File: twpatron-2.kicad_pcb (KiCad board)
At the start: 4 copper layers, 38.1 x 21 mm, 12 parts, among them J1 Conn_01x04, J3 SMP-straight-19S141-40ML5, J6 Conn_01x04, U1 MM5800, U2 MM5800, U3 MM5800, U4 MM5800

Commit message: a full draft of pcb is essentially done now
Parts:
- added ?: , , F.Cu at (149.4, 74.3)
- J3: footprint rosenberger-smp:rosenberger-19S141-40ML5 -> molex-smp:MOLEX_85305-0232

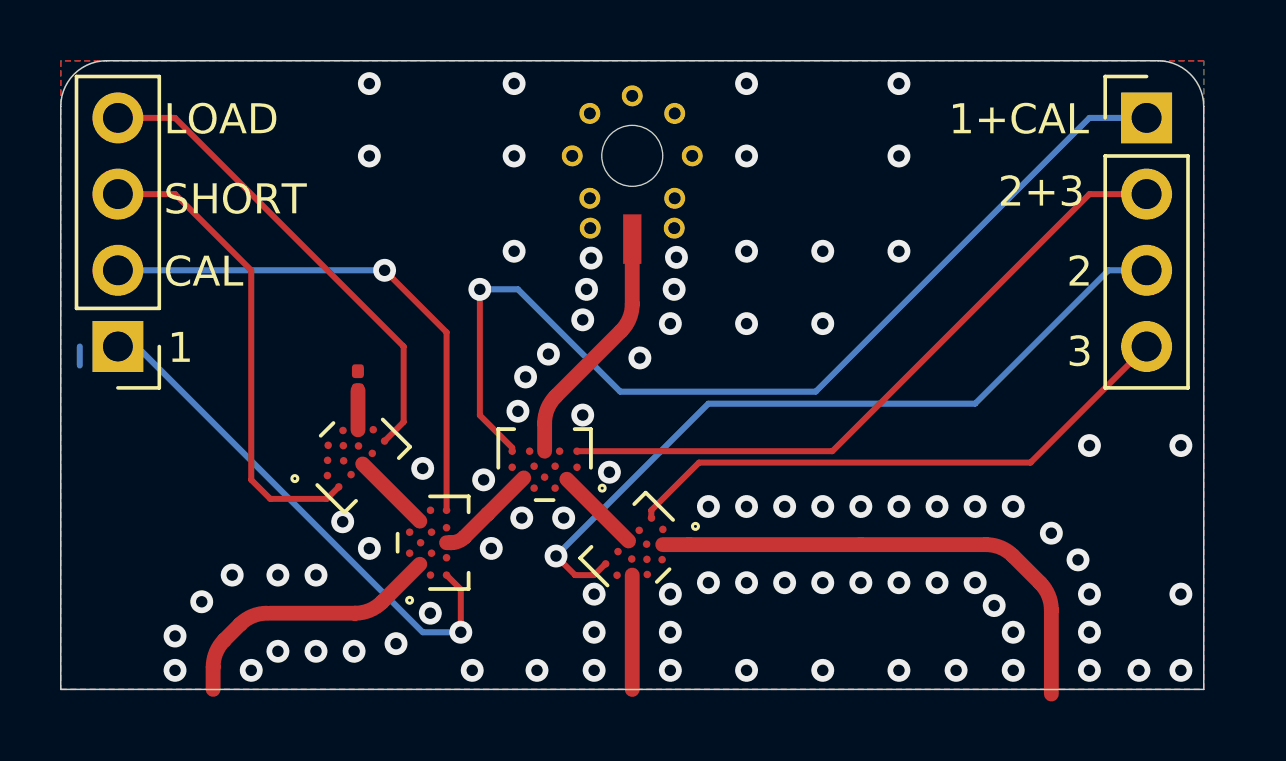
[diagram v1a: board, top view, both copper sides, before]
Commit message: added jaws design, tweaked mechanical for M2.5 screws
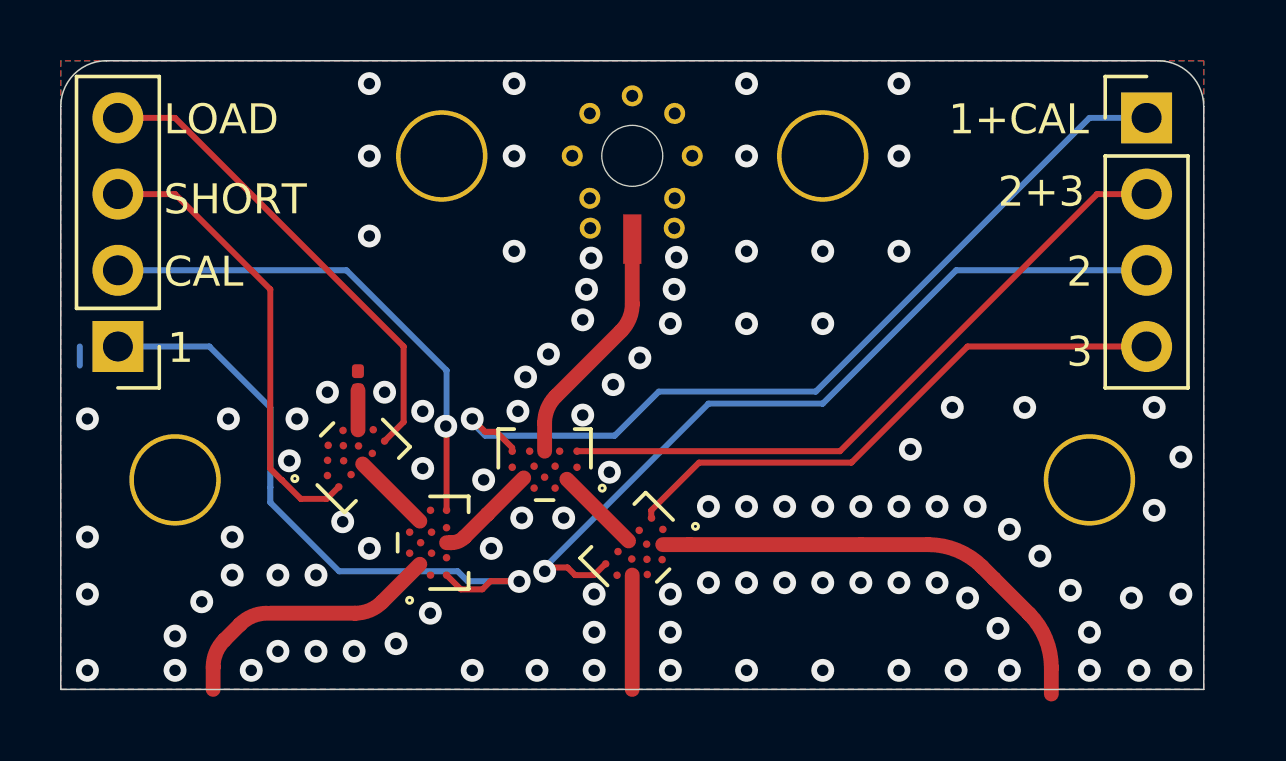
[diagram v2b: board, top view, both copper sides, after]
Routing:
- net Net-(J1-Pin_1): track 33.3 -> 29.0 mm
- net Net-(J6-Pin_1): track 18.1 -> 21.8 mm
- net unconnected-(U2-RF1-PadC3): track 16.9 -> 15.9 mm
- net Net-(J1-Pin_3): track 25.7 -> 26.6 mm
- net Net-(J6-Pin_2): track 17.7 -> 17.0 mm
- net Net-(J6-Pin_3): track 15.8 -> 15.2 mm
- net GND: vias 87 -> 103

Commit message: changed to stackup like JAWS
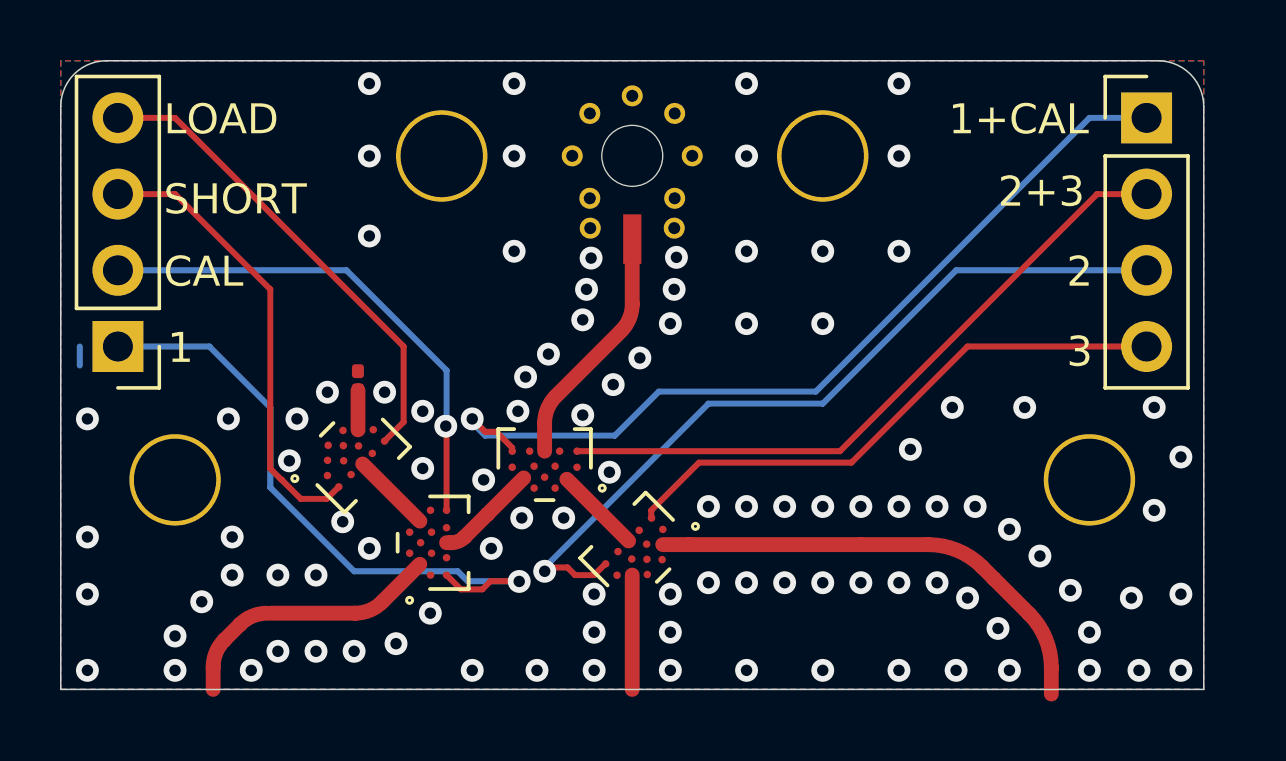
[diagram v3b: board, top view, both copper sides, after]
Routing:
- removed copper zone on In1.Cu, net GND
- removed copper zone on In2.Cu, net GND
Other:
- copper layers 4 -> 2
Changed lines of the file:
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@@
 	(generator_version "9.0")
 	(general
-		(thickness 1.125199)
+		(thickness 0.598)
 		(legacy_teardrops no)
 	)
@@
 	(layers
 		(0 "F.Cu" signal "Top Layer")
-		(4 "In1.Cu" signal "Mid-Layer 1")
-		(6 "In2.Cu" signal "Mid-Layer 2")
 		(2 "B.Cu" signal "Bottom Layer")
 		(9 "F.Adhes" user "F.Adhesive")
@@
 			(layer "F.Mask"
 				(type "Top Solder Mask")
+				(color "Green")
 				(thickness 0.01)
 			)
@@
 			(layer "dielectric 1"
 				(type "core")
-				(thickness 0.321733)
-				(material "FR4")
-				(epsilon_r 4.5)
-				(loss_tangent 0.02)
-			)
-			(layer "In1.Cu"
-				(type "copper")
-				(thickness 0.035)
-			)
-			(layer "dielectric 2"
-				(type "prepreg")
-				(thickness 0.321733)
-				(material "FR4")
-				(epsilon_r 4.5)
-				(loss_tangent 0.02)
-			)
-			(layer "In2.Cu"
-				(type "copper")
-				(thickness 0.035)
-			)
-			(layer "dielectric 3"
-				(type "core")
-				(thickness 0.321733)
-				(material "FR4")
-				(epsilon_r 4.5)
-				(loss_tangent 0.02)
+				(color "FR4 natural")
+				(thickness 0.508)
+				(material "RO4350B")
+				(epsilon_r 3.48)
+				(loss_tangent 0)
 			)
 			(layer "B.Cu"
@@
 			(layer "B.Mask"
 				(type "Bottom Solder Mask")
+				(color "Green")
 				(thickness 0.01)
 			)
@@
 	)
 	(segment
-		(start 137.3111 85.3176)
-		(end 137.3117 85.317)
-		(width 0.2)
-		(layer "B.Cu")
-		(net 7)
-	)
-	(segment
-		(start 145.608069 88.450092)
-		(end 145.599777 88.4418)
+		(start 140.1051 88.1116)
+		(end 137.3111 85.3176)
 		(width 0.2)
 		(layer "B.Cu")
@@
 	)
 	(segment
-		(start 137.3111 85.817422)
-		(end 137.3111 85.3176)
+		(start 143.8897 88.4418)
+		(end 143.5595 88.1116)
 		(width 0.2)
 		(layer "B.Cu")
@@
 	)
 	(segment
-		(start 139.605278 88.1116)
-		(end 137.3111 85.817422)
+		(start 145.608069 88.450092)
+		(end 145.599777 88.4418)
 		(width 0.2)
 		(layer "B.Cu")
@@
 	)
 	(segment
-		(start 143.5595 88.1116)
-		(end 139.605278 88.1116)
+		(start 137.3111 85.3176)
+		(end 137.3117 85.317)
 		(width 0.2)
 		(layer "B.Cu")
@@
 	)
 	(segment
-		(start 135.2791 80.6186)
-		(end 132.2311 80.6186)
+		(start 130.9611 81.2536)
+		(end 130.9611 80.6186)
 		(width 0.2)
 		(layer "B.Cu")
@@
 	)
 	(segment
-		(start 130.9611 81.2536)
-		(end 130.9611 80.6186)
+		(start 137.3117 85.317)
+		(end 137.3117 82.6512)
 		(width 0.2)
 		(layer "B.Cu")
@@
 	)
 	(segment
-		(start 137.3117 85.317)
-		(end 137.3117 82.6512)
+		(start 143.5595 88.1116)
+		(end 140.1051 88.1116)
 		(width 0.2)
 		(layer "B.Cu")
@@
 	)
 	(segment
-		(start 143.8897 88.4418)
-		(end 143.5595 88.1116)
+		(start 135.2791 80.6186)
+		(end 132.2311 80.6186)
 		(width 0.2)
 		(layer "B.Cu")
@@
 		(net 10)
 		(net_name "GND")
-		(layers "F.Cu" "B.Cu" "In1.Cu" "In2.Cu")
+		(layers "F.Cu" "B.Cu")
 		(hatch edge 0.5)
 		(connect_pads yes
@@
 		(net 0)
 		(net_name "")
-		(layers "F.Cu" "B.Cu" "In1.Cu" "In2.Cu" "User.11")
+		(layers "F.Cu" "B.Cu" "User.11")
 		(hatch edge 0.5)
 		(connect_pads
@@
 		(hatch edge 0.5)
 		(connect_pads
+			(clearance 0)
+		)
+		(min_thickness 0.25)
+		(filled_areas_thickness no)
+		(fill yes
+			(thermal_gap 0.5)
+			(thermal_bridge_width 0.5)
+		)
+		(polygon
+			(pts
+				(xy 143.0261 89.1276) (xy 146.8361 89.1276) (xy 146.8361 92.0486) (xy 143.0261 92.0486)
+			)
+		)
+	)
+	(zone
+		(net 0)
+		(net_name "")
+		(layer "F.Mask")
+		(hatch edge 0.5)
+		(connect_pads
 			(clearance 0.1524)
 		)
@@
 		(polygon
 			(pts
-				(xy 130.3261 85.0636) (xy 130.3261 82.3966) (xy 136.2951 82.3966) (xy 136.2951 85.0636)
+				(xy 130.3261 85.0636) (xy 130.3261 82.3966) (xy 136.9301 82.3966) (xy 136.9301 85.0636)
 			)
 		)
@@
 		(polygon
 			(pts
-				(xy 144.0421 88.6196) (xy 145.8201 88.6196) (xy 145.8201 87.4766) (xy 146.7091 86.5876) (xy 146.7091 85.8256)
+				(xy 144.0421 88.1116) (xy 145.1851 88.1116) (xy 145.8201 87.4766) (xy 146.7091 86.5876) (xy 146.7091 85.8256)
 				(xy 146.0741 85.8256) (xy 144.8041 84.6826) (xy 144.0421 84.6826)
 			)
@@
 		(polygon
 			(pts
-				(xy 144.4231 92.0486) (xy 144.4231 88.6196) (xy 150.6461 88.6196) (xy 150.6461 86.0796) (xy 168.4261 86.0796)
+				(xy 146.8361 92.0486) (xy 146.8361 88.6196) (xy 150.6461 88.6196) (xy 150.6461 86.0796) (xy 168.4261 86.0796)
 				(xy 168.4261 92.0486)
 			)
@@
 		(polygon
 			(pts
-				(xy 130.3261 86.0796) (xy 130.3261 85.0636) (xy 136.2951 85.0636) (xy 137.3111 86.0796)
+				(xy 130.3261 86.0796) (xy 130.3261 85.0636) (xy 136.9301 85.0636) (xy 137.9461 86.0796)
 			)
 		)
@@
 		(hatch edge 0.5)
 		(connect_pads
-			(clearance 0.1524)
-		)
-		(min_thickness 0.25)
-		(filled_areas_thickness no)
-		(fill yes
-			(thermal_gap 0.5)
-			(thermal_bridge_width 0.5)
-		)
-		(polygon
-			(pts
-				(xy 143.6611 92.0486) (xy 143.6611 90.9056) (xy 142.1371 90.9056) (xy 133.8821 82.5236) (xy 130.3261 82.5236)
-				(xy 130.3261 92.0486)
-			)
-		)
-	)
-	(zone
-		(net 0)
-		(net_name "")
-		(layer "In1.Cu")
-		(hatch edge 0.5)
-		(connect_pads
 			(clearance 0)
 		)
 		(min_thickness 0.25)
 		(filled_areas_thickness no)
-		(keepout
-			(tracks allowed)
-			(vias allowed)
-			(pads allowed)
-			(copperpour not_allowed)
-			(footprints allowed)
-		)
-		(placement
-			(enabled no)
-			(sheetname "")
-		)
-		(fill
-			(thermal_gap 0.5)
-			(thermal_bridge_width 0.5)
-		)
-		(polygon
-			(pts
-				(arc
-					(start 149.3634 72.6303)
-					(mid 148.186986 73.117586)
-					(end 147.6997 74.294)
-				)
-				(arc
-					(start 147.6997 74.294)
-					(mid 148.186986 75.470414)
-					(end 149.3634 75.9577)
-				)
-				(arc
-					(start 149.3634 75.9577)
-					(mid 150.539814 75.470414)
-					(end 151.0271 74.294)
-				)
-				(arc
-					(start 151.0271 74.294)
-					(mid 150.539814 73.117586)
-					(end 149.3634 72.6303)
-				)
-			)
-		)
-	)
-	(zone
-		(net 0)
-		(net_name "")
-		(layers "In1.Cu" "In2.Cu")
-		(hatch edge 0.5)
-		(connect_pads
-			(clearance 0)
-		)
-		(min_thickness 0.25)
-		(filled_areas_thickness no)
-		(keepout
-			(tracks allowed)
-			(vias allowed)
-			(pads allowed)
-			(copperpour not_allowed)
-			(footprints allowed)
-		)
-		(placement
-			(enabled no)
-			(sheetname "")
-		)
-		(fill
+		(fill yes
 			(thermal_gap 0.5)
 			(thermal_bridge_width 0.5)
@@
 		(polygon
 			(pts
-				(xy 148.8173 78.0024) (xy 148.8173 74.294) (xy 149.9349 74.294) (xy 149.9349 78.0024)
+				(xy 133.8821 82.5236) (xy 136.6761 82.5236) (xy 137.0571 82.9046) (xy 137.0571 85.6986)
 			)
 		)
@@
 		(net 0)
 		(net_name "")
-		(layers "In1.Cu" "In2.Cu")
+		(layer "B.Mask")
 		(hatch edge 0.5)
 		(connect_pads
-			(clearance 0)
+			(clearance 0.1524)
 		)
 		(min_thickness 0.25)
 		(filled_areas_thickness no)
-		(keepout
-			(tracks allowed)
-			(vias allowed)
-			(pads allowed)
-			(copperpour not_allowed)
-			(footprints allowed)
-		)
-		(placement
-			(enabled no)
-			(sheetname "")
-		)
-		(fill
+		(fill yes
 			(thermal_gap 0.5)
 			(thermal_bridge_width 0.5)
@@
 		(polygon
 			(pts
-				(xy 148.8173 78.0024) (xy 149.9349 78.0024) (xy 149.3761 78.5612)
+				(xy 143.6611 92.0486) (xy 143.6611 90.9056) (xy 142.1371 90.9056) (xy 133.8821 82.5236) (xy 130.3261 82.5236)
+				(xy 130.3261 92.0486)
 			)
 		)

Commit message: twpatron 3d assembly coming together
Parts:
- removed the ? at (149.4, 74.3)
- J3: footprint molex-smp:MOLEX_85305-0232 -> molex-smp:jaws-molex-CONN_73415-3310_MOL
- moved J1 5.72 mm to (160.8, 73.3)
- moved J6 5.72 mm to (137.9, 80.9)
- moved J3 0.64 mm to (149.4, 74.9)
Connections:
- ? pad 8: (no net) -> GND
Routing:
- net Net-(J6-Pin_2): track 17.0 -> 11.2 mm
- net Net-(J1-Pin_4): track 19.0 -> 13.2 mm
- net Net-(J1-Pin_3): track 26.6 -> 20.8 mm
- net Net-(J6-Pin_4): track 16.1 -> 12.4 mm
- net Net-(J1-Pin_1): track 29.0 -> 25.3 mm
- net Net-(J1-Pin_2): track 22.5 -> 18.9 mm
- net Net-(J6-Pin_3): track 15.2 -> 13.1 mm
- net Net-(J6-Pin_1): track 21.6 -> 20.6 mm
- net unconnected-(U2-RF1-PadC3): track 15.9 -> 15.0 mm
- net unconnected-(U3-RF1-PadC3): track 9.18 -> 8.43 mm
- net GND: vias 103 -> 101

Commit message: work on pcb layout, lots of small improvements and tweaks
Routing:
- net GND: vias 101 -> 110
